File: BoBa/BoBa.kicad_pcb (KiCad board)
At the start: 4 copper layers, 90.3 x 95.8 mm, 41 parts, among them J1 DF13C-2P-1.25V(21), J2 DF13C-2P-1.25V(21), J3 DF13C-2P-1.25V(21), J4 DF13C-2P-1.25V(21), Q1 FQD13N06LTM, Q2 FQD13N06LTM, U1 LTC4231HUD-2#TRPBF, U2 INA219, U3 INA219AIDCNR, U4_IN-A LTC4231IUD-2#TRPBF, U5 INA219AIDCNR

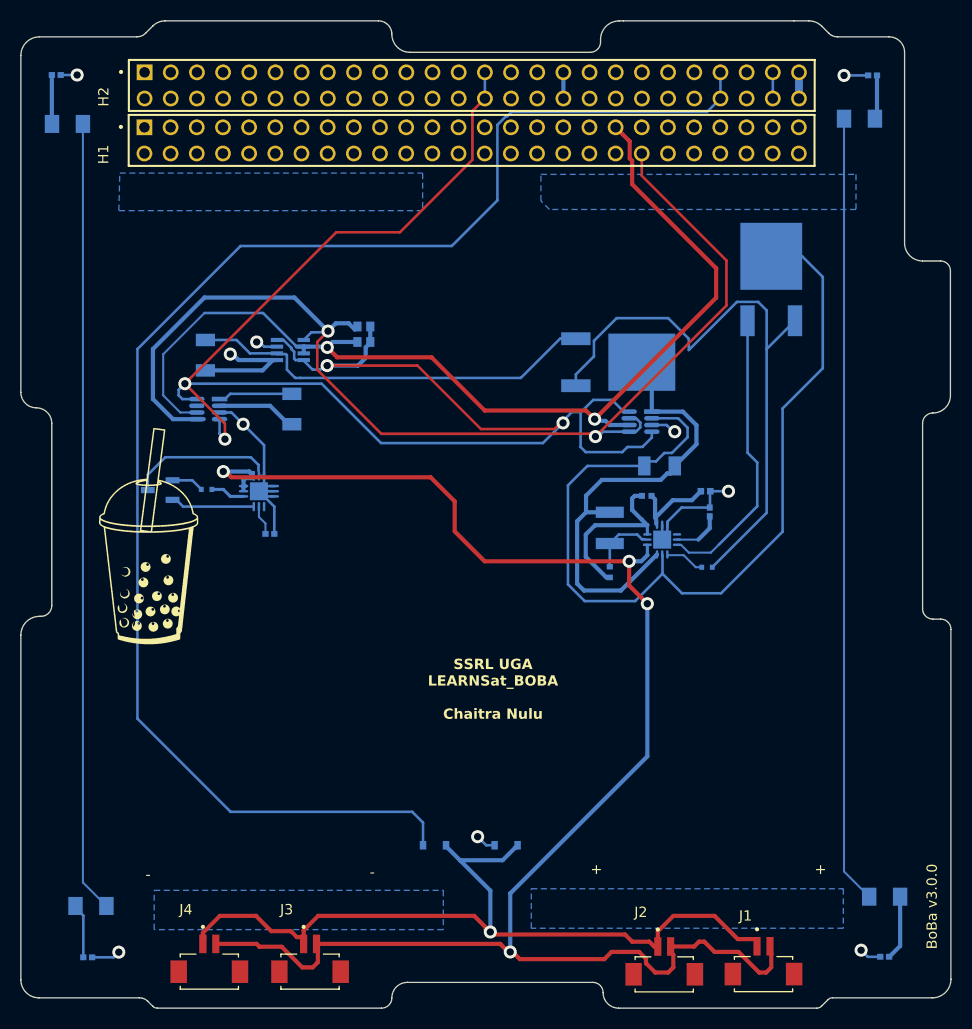
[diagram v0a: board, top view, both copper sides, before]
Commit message: Updated footprint mappings and reduce DRC violations. Currently at 26 warnings
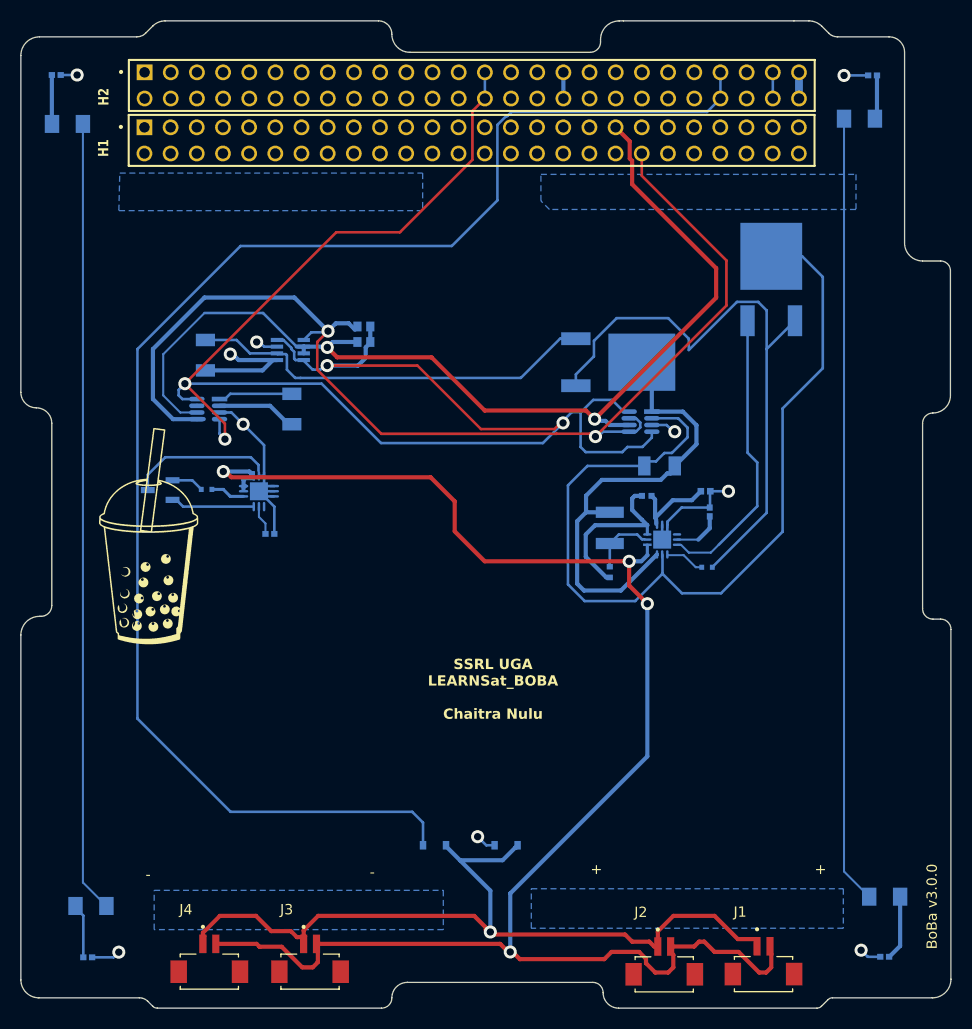
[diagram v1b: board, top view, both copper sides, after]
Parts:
- H1, H2: footprint SnapEDA_Library:SAMTEC_SSQ-126-X-G-D -> Vault:SAMTEC_SSQ-126-X-G-D
- J1, J2, J3, J4: footprint DF13C-2P-1.25V(21):HRS_DF13C-2P-1.25V(21) -> Vault:HRS_DF13C-2P-1.25V(21)
- Q2: footprint FQD13N06LTM:TO229P991X239-3N -> Vault:TO229P991X239-3N
- R1: footprint SnapEDA_Library:RESC3225X60N -> Vault:RESC3225X60N
- U2: footprint SnapEDA_Library:SOT23-8 -> Vault:SOT23-8

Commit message: fixed all errors
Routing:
- net Pack-_Neg: track 48.0 -> 141.7 mm, vias 0 -> 2
- net Chassis GND: track 153.3 -> 233.5 mm
- net I2C Clock: track 114.5 -> 116.7 mm
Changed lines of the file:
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@@
+	)
+	(segment
+		(start 121.080375 94.45404)
+		(end 121.50559 94.879255)
+		(width 0.2)
+		(layer "B.Cu")
+		(net "I2C Clock")
 	)
 	(segment
@@
 	)
 	(segment
+		(start 121.50559 94.879255)
+		(end 121.50559 95.36523)
+		(width 0.2)
+		(layer "B.Cu")
+		(net "I2C Clock")
+	)
+	(segment
 		(start 133.06362 87.32615)
 		(end 131.56748 87.32615)
@@
 	)
 	(segment
+		(start 120.45297 94.45404)
+		(end 121.080375 94.45404)
+		(width 0.2)
+		(layer "B.Cu")
+		(net "I2C Clock")
+	)
+	(segment
 		(start 121.19049 83.94947)
 		(end 129.92139 83.94947)
@@
 		(end 116.19049 93.798156)
 		(width 0.4064)
+		(layer "B.Cu")
+		(net "I2C Clock")
+	)
+	(segment
+		(start 121.50559 95.36523)
+		(end 121.12607 95.74475)
+		(width 0.2)
 		(layer "B.Cu")
 		(net "I2C Clock")
@@
 	)
 	(segment
+		(start 185.6961 144.44386)
+		(end 185.6961 142.08738)
+		(width 0.2)
+		(layer "B.Cu")
+		(net "Chassis GND")
+	)
+	(segment
+		(start 116.97418 148.28666)
+		(end 181.8533 148.28666)
+		(width 0.2)
+		(layer "B.Cu")
+		(net "Chassis GND")
+	)
+	(segment
+		(start 181.8533 148.28666)
+		(end 185.6961 144.44386)
+		(width 0.2)
+		(layer "B.Cu")
+		(net "Chassis GND")
+	)
+	(segment
 		(start 111.67642 142.9889)
 		(end 109.39711 140.70959)
@@
 	)
 	(segment
+		(start 111.67642 142.9889)
+		(end 116.97418 148.28666)
+		(width 0.2)
+		(layer "B.Cu")
+		(net "Chassis GND")
+	)
+	(segment
 		(start 127.11108 105.87006)
 		(end 126.47608 105.23506)
@@
 	)
 	(segment
+		(start 149.19049 103.44947)
+		(end 144.69049 98.94947)
+		(width 0.2)
+		(layer "F.Cu")
+		(net "Pack-_Neg")
+	)
+	(segment
+		(start 130.69049 95.94947)
+		(end 130.69049 85.94947)
+		(width 0.2)
+		(layer "F.Cu")
+		(net "Pack-_Neg")
+	)
+	(segment
+		(start 148.19049 81.94947)
+		(end 151.94049 85.69947)
+		(width 0.2)
+		(layer "F.Cu")
+		(net "Pack-_Neg")
+	)
+	(segment
+		(start 130.69049 85.94947)
+		(end 134.69049 81.94947)
+		(width 0.2)
+		(layer "F.Cu")
+		(net "Pack-_Neg")
+	)
+	(segment
+		(start 134.69049 81.94947)
+		(end 148.19049 81.94947)
+		(width 0.2)
+		(layer "F.Cu")
+		(net "Pack-_Neg")
+	)
+	(segment
+		(start 144.69049 98.94947)
+		(end 133.69049 98.94947)
+		(width 0.2)
+		(layer "F.Cu")
+		(net "Pack-_Neg")
+	)
+	(segment
+		(start 133.69049 98.94947)
+		(end 130.69049 95.94947)
+		(width 0.2)
+		(layer "F.Cu")
+		(net "Pack-_Neg")
+	)
+	(via
+		(at 149.19049 103.44947)
+		(size 0.6)
+		(drill 0.3)
+		(layers "F.Cu" "B.Cu")
+		(net "Pack-_Neg")
+	)
+	(via
+		(at 151.94049 85.69947)
+		(size 0.6)
+		(drill 0.3)
+		(layers "F.Cu" "B.Cu")
+		(net "Pack-_Neg")
+	)
+	(segment
 		(start 155.69531 87.94465)
-		(end 151.88803 91.75193)
+		(end 153.19049 90.44947)
 		(width 0.254)
 		(layer "B.Cu")
@@
 	)
 	(segment
+		(start 153.19049 90.44947)
+		(end 151.88803 91.75193)
+		(width 0.254)
+		(layer "B.Cu")
+		(net "Pack-_Neg")
+	)
+	(segment
+		(start 125.97608 106.94607)
+		(end 125.97608 104.23719)
+		(width 0.2)
+		(layer "B.Cu")
+		(net "Pack-_Neg")
+	)
+	(segment
 		(start 118.46908 103.58515)
 		(end 119.12111 104.23719)
@@
 	)
 	(segment
+		(start 129.47948 110.44947)
+		(end 125.97608 106.94607)
+		(width 0.2)
+		(layer "B.Cu")
+		(net "Pack-_Neg")
+	)
+	(segment
 		(start 119.12111 104.23719)
 		(end 125.94588 104.23719)
@@
 	)
 	(segment
+		(start 149.19049 106.94947)
+		(end 145.69049 110.44947)
+		(width 0.2)
+		(layer "B.Cu")
+		(net "Pack-_Neg")
+	)
+	(segment
 		(start 129.097441 89.44089)
 		(end 128.29871 89.44089)
@@
 	)
 	(segment
+		(start 153.19049 86.94947)
+		(end 153.19049 90.44947)
+		(width 0.2)
+		(layer "B.Cu")
+		(net "Pack-_Neg")
+	)
+	(segment
+		(start 151.94049 85.69947)
+		(end 153.19049 86.94947)
+		(width 0.2)
+		(layer "B.Cu")
+		(net "Pack-_Neg")
+	)
+	(segment
 		(start 118.09408 103.58515)
 		(end 118.46908 103.58515)
@@
 	)
 	(segment
+		(start 149.19049 103.44947)
+		(end 149.19049 106.94947)
+		(width 0.2)
+		(layer "B.Cu")
+		(net "Pack-_Neg")
+	)
+	(segment
 		(start 129.19049 90.94947)
 		(end 129.99295 91.75193)
@@
 		(layer "B.Cu")
 		(net "Pack-_Neg")
+	)
+	(segment
+		(start 145.69049 110.44947)
+		(end 129.47948 110.44947)
+		(width 0.2)
+		(layer "B.Cu")
+		(net "Pack-_Neg")

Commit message: fixed errors, changes some traces, 33 warnings remaining
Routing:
- net INHIBIT: track 162.7 -> 161.0 mm
- net I2C Clock: track 116.7 -> 117.8 mm
